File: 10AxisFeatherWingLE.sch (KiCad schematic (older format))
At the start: 23 parts, among them J1 feather long, J2 feather short, J3 feather long, J4 feather short, J5 feather breakout, J6 stemma connector, U1 LSM9DS1, U2 BMP280

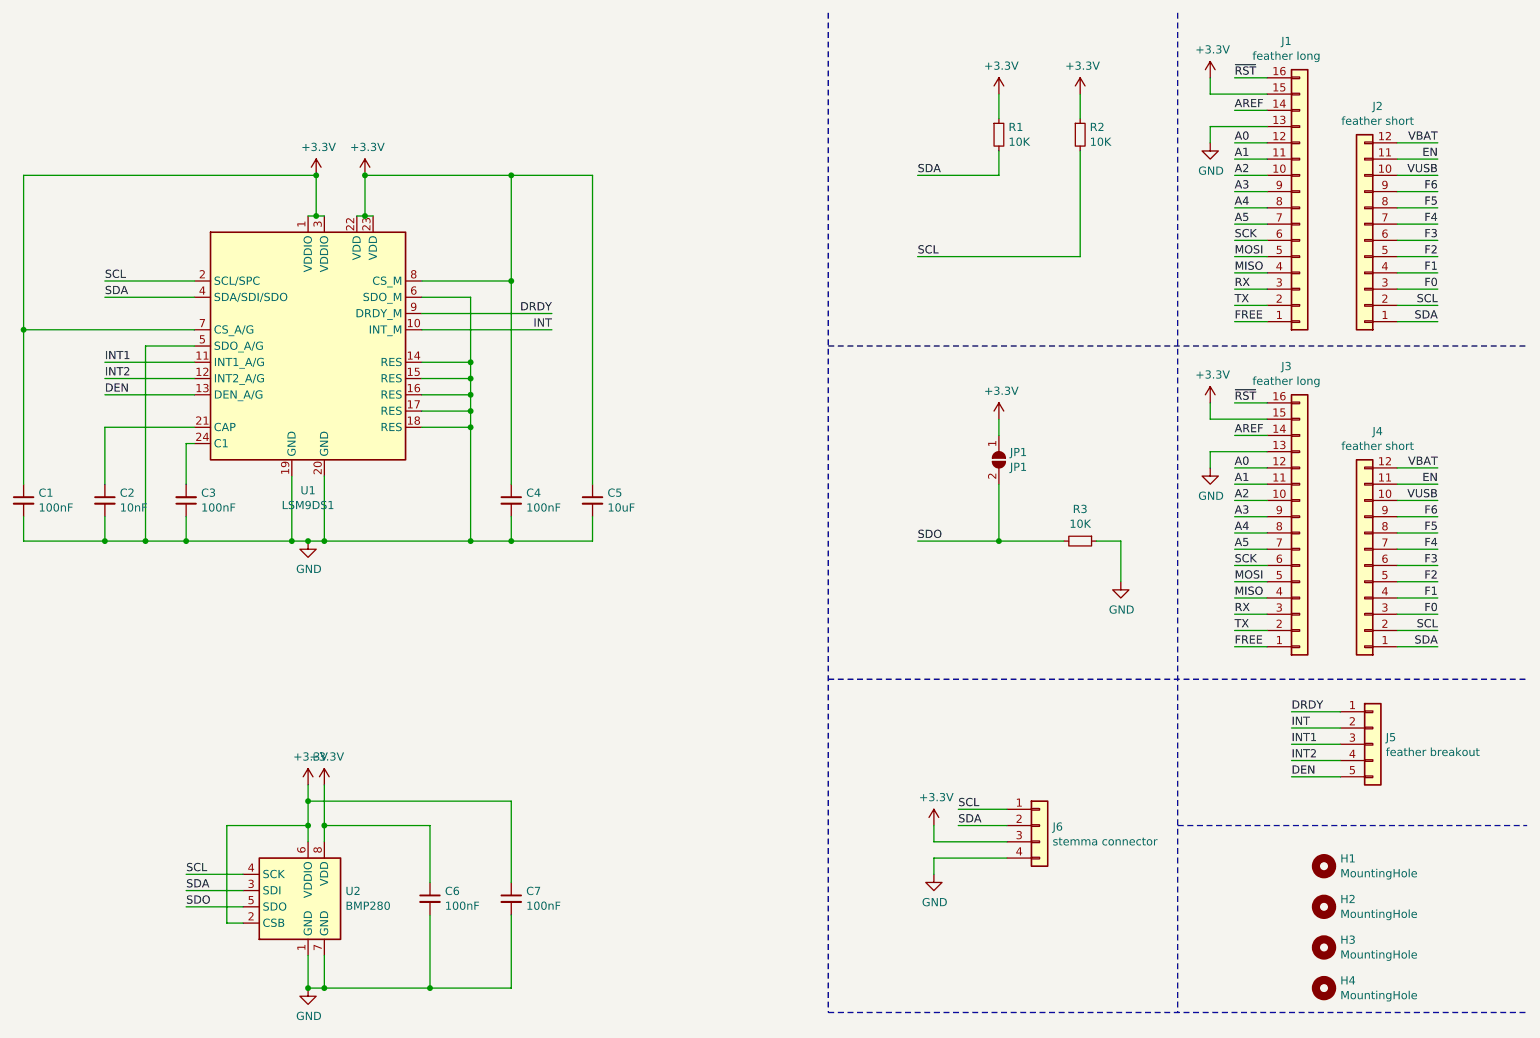
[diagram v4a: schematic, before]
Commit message: Removed STEMMA connector
STEMMA requires the use of a 3.3V to 5V level shifter and voltage regulator.
The board does not support these features, so they were removed.
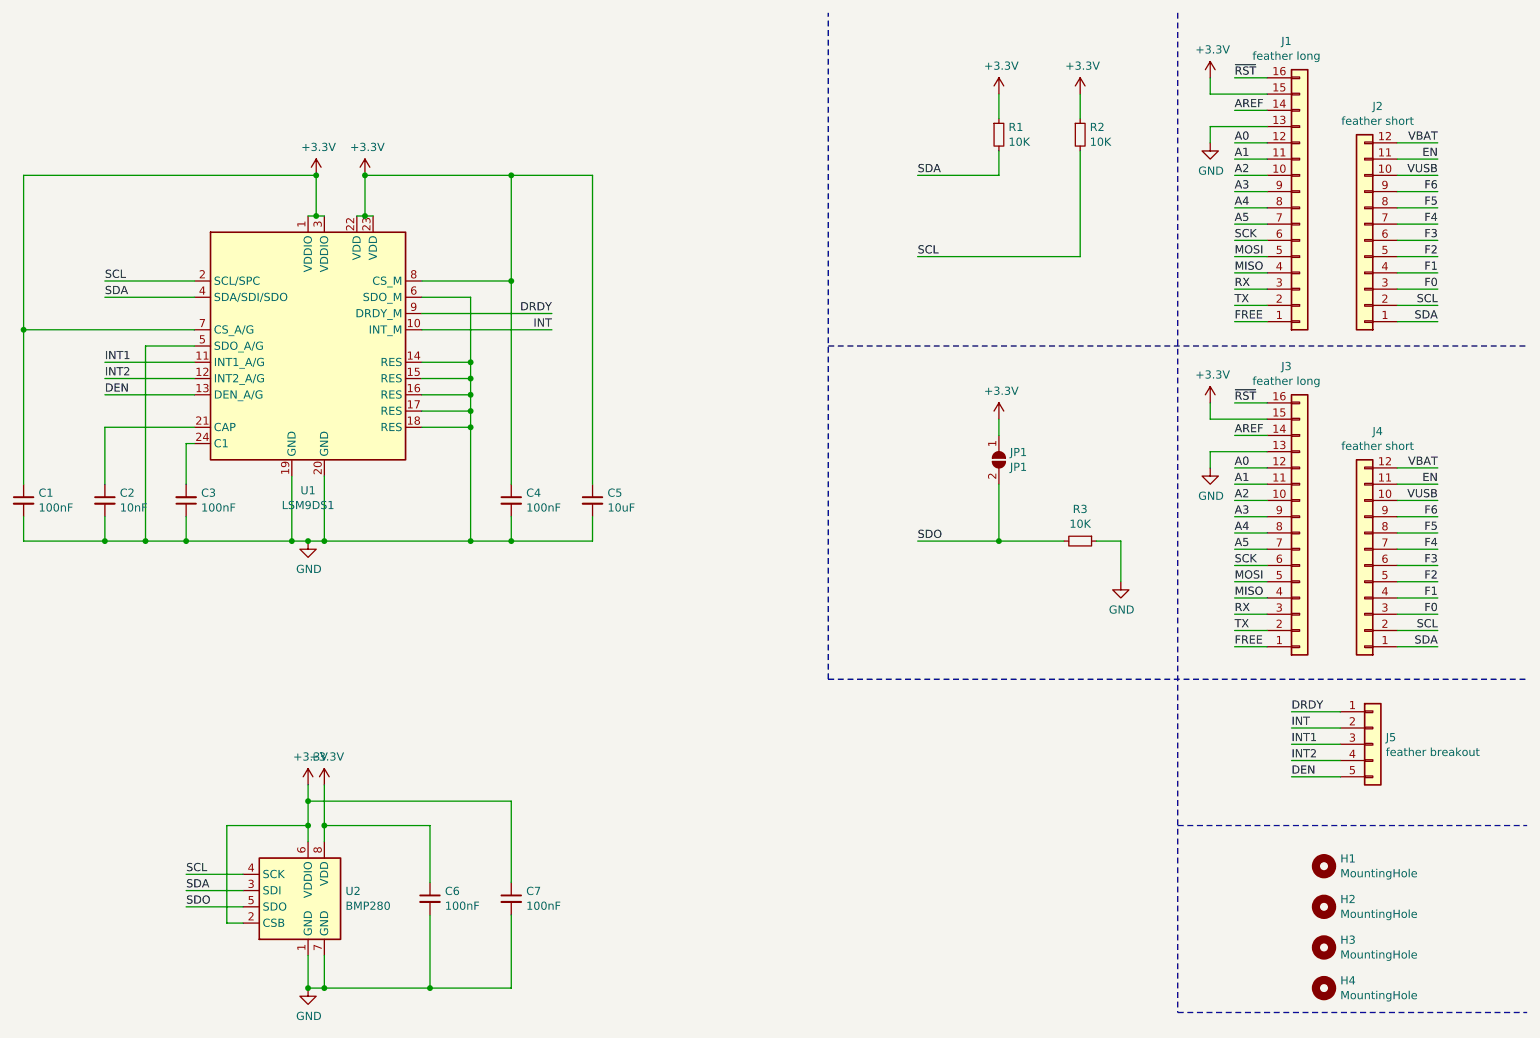
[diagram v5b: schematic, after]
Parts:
- removed J6: stemma connector, Connector_JST:JST_PH_B4B-PH-K_1x04_P2.00mm_Vertical, symbol Connector_Generic:Conn_01x04
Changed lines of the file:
@@
 Wire Notes Line
 	6200 4600 10500 4600
-Wire Notes Line
-	6200 6650 10500 6650
-Wire Notes Line
-	6200 500  6200 6650
 $Comp
 L Connector_Generic:Conn_01x16 J3
@@
 Text Label 6750 3750 0    50   ~ 0
 SDO
-$Comp
-L Connector_Generic:Conn_01x04 J6
-U 1 1 5E2B8C1A
-P 7500 5500
-F 0 "J6" H 7580 5492 50  0000 L CNN
-F 1 "stemma connector" H 7580 5401 50  0000 L CNN
-F 2 "Connector_JST:JST_PH_B4B-PH-K_1x04_P2.00mm_Vertical" H 7500 5500 50  0001 C CNN
-F 3 "~" H 7500 5500 50  0001 C CNN
-	1    7500 5500
-	1    0    0    -1
-$EndComp
 Wire Wire Line
 	9050 4800 9350 4800
@@
 Wire Wire Line
 	9050 5200 9350 5200
-Wire Wire Line
-	7000 5400 7300 5400
-Wire Wire Line
-	7000 5500 7300 5500
-Text Label 7000 5400 0    50   ~ 0
-SCL
-Text Label 7000 5500 0    50   ~ 0
-SDA
-Wire Wire Line
-	6850 5600 6850 5500
-Wire Wire Line
-	6850 5600 7300 5600
-Wire Wire Line
-	6850 5700 6850 5800
-Wire Wire Line
-	6850 5700 7300 5700
-$Comp
-L power:+3.3V #PWR014
-U 1 1 5E330536
-P 6850 5500
-F 0 "#PWR014" H 6850 5350 50  0001 C CNN
-F 1 "+3.3V" H 6865 5673 50  0000 C CNN
-F 2 "" H 6850 5500 50  0001 C CNN
-F 3 "" H 6850 5500 50  0001 C CNN
-	1    6850 5500
-	1    0    0    -1
-$EndComp
-$Comp
-L power:GND #PWR015
-U 1 1 5E330953
-P 6850 5800
-F 0 "#PWR015" H 6850 5550 50  0001 C CNN
-F 1 "GND" H 6855 5627 50  0000 C CNN
-F 2 "" H 6850 5800 50  0001 C CNN
-F 3 "" H 6850 5800 50  0001 C CNN
-	1    6850 5800
-	1    0    0    -1
-$EndComp
 $Comp
 L Mechanical:MountingHole H1
@@
 Wire Notes Line
 	8350 5500 10500 5500
+Wire Notes Line
+	8350 6650 10500 6650
+Wire Notes Line
+	6200 4600 6200 500
 $EndSCHEMATC
